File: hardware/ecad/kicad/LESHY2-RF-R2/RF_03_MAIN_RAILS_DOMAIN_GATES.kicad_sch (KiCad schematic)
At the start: 69 parts, among them Q4 Diodes Incorporated MMBT3904-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, U13 Texas Instruments TPS629203DR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, U14 Texas Instruments TPS25961DRVR, U15 Texas Instruments SN74LVC2G08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, U16 Texas Instruments TPS564252DR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, U17 Texas Instruments TPS259470LR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, U18 SN74LVC1G07DCKR, U19 74LVC1G32GV,125, U20 Texas Instruments TPS564252DR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, U21 Texas Instruments TPS25974LRP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

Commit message: Complete current R2 schematic and sourcing revalidation
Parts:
- added C70: CL05B104KB5NNNC, Capacitor_SMD:C_0402_1005Metric, symbol Leshy2_R2:samsung_cl05b104kb5nnnc
- added C71: CL10B105KO8NNNC, Capacitor_SMD:C_0603_1608Metric, symbol Leshy2_R2:samsung_cl10b105ko8nnnc
- added C78, C79, C82: Murata GRM32ER71E226KE15L, Capacitor_SMD:C_1210_3225Metric, symbol Leshy2_R2:murata_grm32er71e226ke15l
- added R62: Yageo RC0402JR-070RL, Resistor_SMD:R_0402_1005Metric, symbol Leshy2_R2:yageo_rc0402jr_070rl
- added TP1: LESHY2-PCB-TP-1MM-R2, Leshy2_R2:PCB_TestPoint_Pad_D1.0mm, symbol Leshy2_R2:leshy2_pcb_testpoint_pad_1mm_r2
- U20: value Texas Instruments TPS564252DRLR -> TPS566231PRQFR; footprint Package_TO_SOT_SMD:Texas_R-PDSO-N6_DRL-6 -> Leshy2_R2:Texas_RQF0009A_1.5x2.0mm; symbol Leshy2_R2:ti_tps564252_drlr -> Leshy2_R2:ti_tps566231p_rqfr
- U22: renamed from L4; value Sunlord MWSA0503S-3R3MT -> PSPMAA0605H-2R2M-ANP; footprint Inductor_SMD:L_Sunlord_MWSA0503S -> Leshy2_R2:PRODTech_PSPMAA0605H_7.1x6.6mm; symbol Leshy2_R2:sunlord_mwsa0503s_3r3mt -> Leshy2_R2:prodtech_pspmaa0605h_2r2m_anp
- renumbered C70 to C72, C71 to C73, C72 to C74, C73 to C75, C74 to C76, C75 to C77, C76 to C80, C77 to C81, C78 to C83, C79 to C84, R62 to R63, R63 to R64, R64 to R65, R65 to R66, R66 to R67, R67 to R68, R68 to R69, R69 to R70, R70 to R71, R71 to R72, R72 to R73, R73 to R74
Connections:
- net MAIN_3V3_FB: now also U20.2 (FB); no longer U20.6 (FB)
- net MAIN_BUCK_SW: now also U20.8 (SW), R62.2 (END_2); no longer U20.2 (SW)
- net MAIN_RAW_3V3: now also C82.1 (END_1)
- net NVDC_SYS: now also U20.5 (VIN_1), U20.6 (VIN_2), C78.1 (END_1), C79.1 (END_1); no longer U20.1 (VIN)
- net POR_N: now also U20.3 (EN); no longer U20.5 (EN)
- net POWER_GROUND: now also U20.4 (PGND), C71.2 (END_2), C78.2 (END_2), C79.2 (END_2), C82.2 (END_2); no longer U20.3 (GND)
- new net MAIN_BUCK_BST: C70.1 (END_1), U20.7 (BST)
- new net MAIN_BUCK_BST_LINK: C70.2 (END_2), R62.1 (END_1)
- new net MAIN_BUCK_VCC: C71.1 (END_1), U20.1 (VCC)
- new net MAIN_RAW_3V3_PG_N: TP1.1 (PROBE), U20.9 (PG)
- no-connect marks 4 -> 3
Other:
- moved on the sheet: C72, C73, C74, C75, C76, C77, C80, C81, C83, C84, L2, L3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

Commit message: Canonicalize physical ground anchors
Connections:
- net SAFETY_GROUND is gone; now on net POWER_GROUND: C58.2 (END_2), C65.2 (END_2), C69.2 (END_2), C83.2 (END_2), C84.2 (END_2), R49.2 (END_2), R71.2 (END_2), R73.2 (END_2), U15.4 (GND), U18.3 (GND), U19.3 (GND)
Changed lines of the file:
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@@
 		(effects (font (size 1.27 1.27)))
 	)
-	(hierarchical_label "SAFETY_GROUND"
-		(shape bidirectional)
+	(label "POWER_GROUND"
 		(at 441.96 50.80 180)
 		(effects (font (size 1.27 1.27)) (justify right bottom))
@@
 		(effects (font (size 1.27 1.27)))
 	)
-	(label "SAFETY_GROUND"
+	(label "POWER_GROUND"
 		(at 1082.04 50.80 180)
 		(effects (font (size 1.27 1.27)) (justify right bottom))
@@
 		(effects (font (size 1.27 1.27)))
 	)
-	(label "SAFETY_GROUND"
+	(label "POWER_GROUND"
 		(at 350.52 86.36 180)
 		(effects (font (size 1.27 1.27)) (justify right bottom))
@@
 		(effects (font (size 1.27 1.27)))
 	)
-	(label "SAFETY_GROUND"
+	(label "POWER_GROUND"
 		(at 533.40 121.92 180)
 		(effects (font (size 1.27 1.27)) (justify right bottom))
@@
 		(effects (font (size 1.27 1.27)))
 	)
-	(label "SAFETY_GROUND"
+	(label "POWER_GROUND"
 		(at 624.84 121.92 180)
 		(effects (font (size 1.27 1.27)) (justify right bottom))
@@
 		(effects (font (size 1.27 1.27)))
 	)
-	(label "SAFETY_GROUND"
+	(label "POWER_GROUND"
 		(at 350.52 157.48 180)
 		(effects (font (size 1.27 1.27)) (justify right bottom))
@@
 		(effects (font (size 1.27 1.27)))
 	)
-	(label "SAFETY_GROUND"
+	(label "POWER_GROUND"
 		(at 167.64 228.60 180)
 		(effects (font (size 1.27 1.27)) (justify right bottom))
@@
 		(effects (font (size 1.27 1.27)))
 	)
-	(label "SAFETY_GROUND"
+	(label "POWER_GROUND"
 		(at 350.52 228.60 180)
 		(effects (font (size 1.27 1.27)) (justify right bottom))
@@
 		(effects (font (size 1.27 1.27)))
 	)
-	(label "SAFETY_GROUND"
+	(label "POWER_GROUND"
 		(at 767.08 233.68 0)
 		(effects (font (size 1.27 1.27)))
@@
 		(effects (font (size 1.27 1.27)))
 	)
-	(label "SAFETY_GROUND"
+	(label "POWER_GROUND"
 		(at 1041.40 232.41 0)
 		(effects (font (size 1.27 1.27)))
@@
 		(effects (font (size 1.27 1.27)))
 	)
-	(label "SAFETY_GROUND"
+	(label "POWER_GROUND"
 		(at 35.56 267.97 0)
 		(effects (font (size 1.27 1.27)))

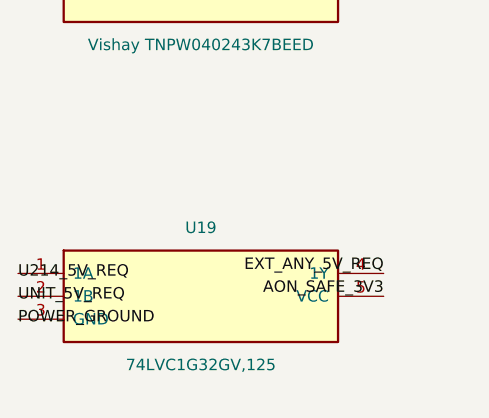
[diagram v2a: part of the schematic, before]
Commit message: Fix exact pin maps and RP flash power; add typed electrical review
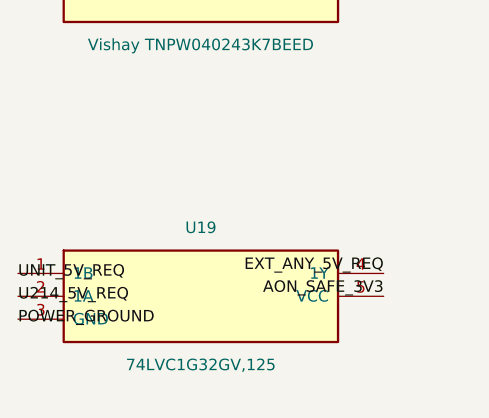
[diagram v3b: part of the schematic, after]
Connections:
- net U214_5V_REQ: now also U19.2 (1A); no longer U19.1 (1A)
- net UNIT_5V_REQ: now also U19.1 (1B); no longer U19.2 (1B)
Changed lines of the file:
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@@
 		)
 	)
-	(label "U214_5V_REQ"
+	(label "UNIT_5V_REQ"
 		(at 35.56 262.89 0)
 		(effects (font (size 1.27 1.27)))
 	)
-	(label "UNIT_5V_REQ"
+	(label "U214_5V_REQ"
 		(at 35.56 265.43 0)
 		(effects (font (size 1.27 1.27)))
